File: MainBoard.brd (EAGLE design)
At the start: 50 x 50 mm, 47 parts, among them U1 STM32F10XRXT6, X1 53261-03, X2 53261-03, X3 53261-03, X4 53261-03, Y1 8MHz, Y2 32.768kHz

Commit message: płytka
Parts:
- removed C1, C14, C2, C3, C4: 100n, rcl:C0805
- removed C6: 10u, rcl:SMC_A
- removed ETRX357: ETRX357HR, etrx357_logical:ETRX3
- removed G1: CR2032V, battery:CR2032V
- removed SW1: (no value), SparkFun-Electromechanical:DIPSWITCH-02
- removed X1, X2, X3, X4: 53261-03, con-molex:53261-03
- added C22: (no value), rcl:C0805
- added IC3: (no value), SparkFun-PowerIC:SOT223
- added JP1: (no value), SparkFun-Connectors:1X06_LONGPADS
- added JP2, JP3: M05X2SHD, SparkFun-Connectors:2X5-SHROUDED
- added JP4: (no value), SparkFun-Connectors:1X04_LONGPADS
- added JP5, JP6, JP7, JP8: (no value), SparkFun-Connectors:1X03_LONGPADS
- added LED5, LED7, LED8, LED9: (no value), led:CHIPLED_0805
- added R10, R12, R13, R14: (no value), resistor:M0805
- added U$1, U$2: (no value), synergia_logo:SYNERGIA_16MM
- C21: value 100n -> (none)
- LED1, LED2, LED3: device SparkFun-LED (1):LED-1206 -> led:CHIPLED_0805
- R6, R7, R8: value 220 -> (none); device rcl:M0805 -> resistor:M0805
- moved C16 106.9 mm to (45.5, 37.1), flipped to the bottom, turned to 270 degrees
- moved R5 103.0 mm to (56.0, 21.5), turned to 90 degrees
- moved C17 102.4 mm to (37.8, 32.9), flipped to the bottom, turned to 270 degrees
- moved C18 101.3 mm to (43.4, 52.5), flipped to the bottom, turned to 270 degrees
- moved C5 93.2 mm to (26.7, 12.7)
- moved R2? 90.3 mm to (44.6, 42.2), flipped to the bottom, turned to 180 degrees
- moved C7 89.7 mm to (17.8, 12.7)
- moved C15 88.9 mm to (33.9, 38.9), flipped to the bottom, turned to 180 degrees
- moved R2 88.0 mm to (60.6, 22.0), turned to 270 degrees
- moved C19 85.6 mm to (39.2, 48.9), flipped to the bottom, turned to 180 degrees
- moved C13 83.9 mm to (40.8, 32.5), flipped to the bottom, turned to 90 degrees
- moved R4 82.9 mm to (40.0, 22.2), turned to 90 degrees
- moved LED1 81.8 mm to (55.9, 55.6), turned to 270 degrees
- moved Y2 74.9 mm to (10.2, 25.4), turned to 270 degrees
- moved R1? 74.7 mm to (35.3, 43.1), flipped to the bottom, turned to 90 degrees
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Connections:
- removed net N$11: LED2.C, R8.2
- removed net N$9: LED3.C, R6.2
- removed net RXD: ETRX357.18
- removed net TXD: ETRX357.17
- new net 5V: C21.1, IC3.3, JP5.1, JP6.1, JP7.1, JP8.1
- new net A1: JP2.7, U1.61
- new net A2: JP2.5, U1.62
- new net A3: JP2.9, U1.58
- new net A4: JP2.2, U1.59
- new net A5: JP2.8, U1.39
- new net A6: JP2.10, U1.40
- new net A7: JP2.4, U1.37
- new net A8: JP2.6, U1.38
- new net L1: R7.1, U1.33
- new net L2: R8.1, U1.9
- new net L4: R10.1, U1.15
- new net L6: R12.1, U1.10
- new net L7: R13.1, U1.11
- new net MISO: JP3.9, U1.22
- new net MOSI: JP3.10, U1.23
- new net N$12: LED7.A, R12.2
- new net N$13: LED8.A, R13.2
- new net N$14: LED9.A, R14.2
- new net REG1: JP5.3, U1.41
- new net REG2: JP6.3, U1.42
- new net REG3: JP7.3, U1.43
- new net REG4: JP8.3, U1.44
- new net RX: JP3.5, U1.17
- new net SCK: JP3.8, U1.21
- new net SWO: JP1.6
- new net TX: JP3.6, U1.16
- net 3.3V: now also C22.1, IC3.2, IC3.4, JP1.1, JP2.1, JP3.2, JP4.2, JP4.3, R14.1, R6.1; no longer C1.1, C14.1, C2.1, C21.1, C3.1, C4.1, C6.+, ETRX357.32, SW1.3, SW1.4
- net GND: now also C22.2, IC3.1, JP1.3, JP2.3, JP3.1, JP5.2, JP6.2, JP7.2, JP8.2, LED1.C, LED2.C, LED3.C, LED5.C, LED7.C, LED8.C, LED9.C; no longer C1.2, C14.2, C2.2, C3.2, C4.2, C6.-, ETRX357.1, ETRX357.13, ETRX357.19, ETRX357.20, ETRX357.31, ETRX357.33, G1.-, R6.1, R7.1, R8.1
- net N$1: now also JP4.1; no longer SW1.1
- net N$10: now also LED5.A, R10.2; no longer LED1.C, R7.2
- net N$2: now also JP4.4; no longer SW1.2
- net N$6: now also R6.2; no longer ETRX357.3
- net N$7: now also R7.2; no longer ETRX357.4
- net N$8: now also R8.2; no longer ETRX357.28
- net NRST: now also JP1.5
- net SCL: now also U1.29
- net SDA: now also U1.30
- net SWCLK: now also JP1.2
- net SWDIO: now also JP1.4
- net V_BATT: no longer G1.+
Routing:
- net 3.3V: track 0.00 -> 251.0 mm, vias 0 -> 2
- net NRST: track 0.00 -> 90.1 mm
- net L2: track 0.00 -> 90.1 mm
- net A2: track 0.00 -> 57.5 mm, vias 0 -> 2
- net BOOT0: track 0.00 -> 48.3 mm, vias 0 -> 2
- net BOOT1: track 0.00 -> 48.0 mm, vias 0 -> 2
- net TX: track 0.00 -> 45.8 mm
- net 5V: track 0.00 -> 45.4 mm
- net A1: track 0.00 -> 45.2 mm, vias 0 -> 2
- net REG1: track 0.00 -> 39.5 mm
- net L7: track 0.00 -> 37.9 mm
- net L4: track 0.00 -> 37.4 mm
- net A4: track 0.00 -> 36.8 mm, vias 0 -> 2
- net REG4: track 0.00 -> 36.4 mm
- net REG2: track 0.00 -> 35.9 mm
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- added copper zone on layer 1, net GND
- added copper zone on layer 16, net GND
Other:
- board outline removed

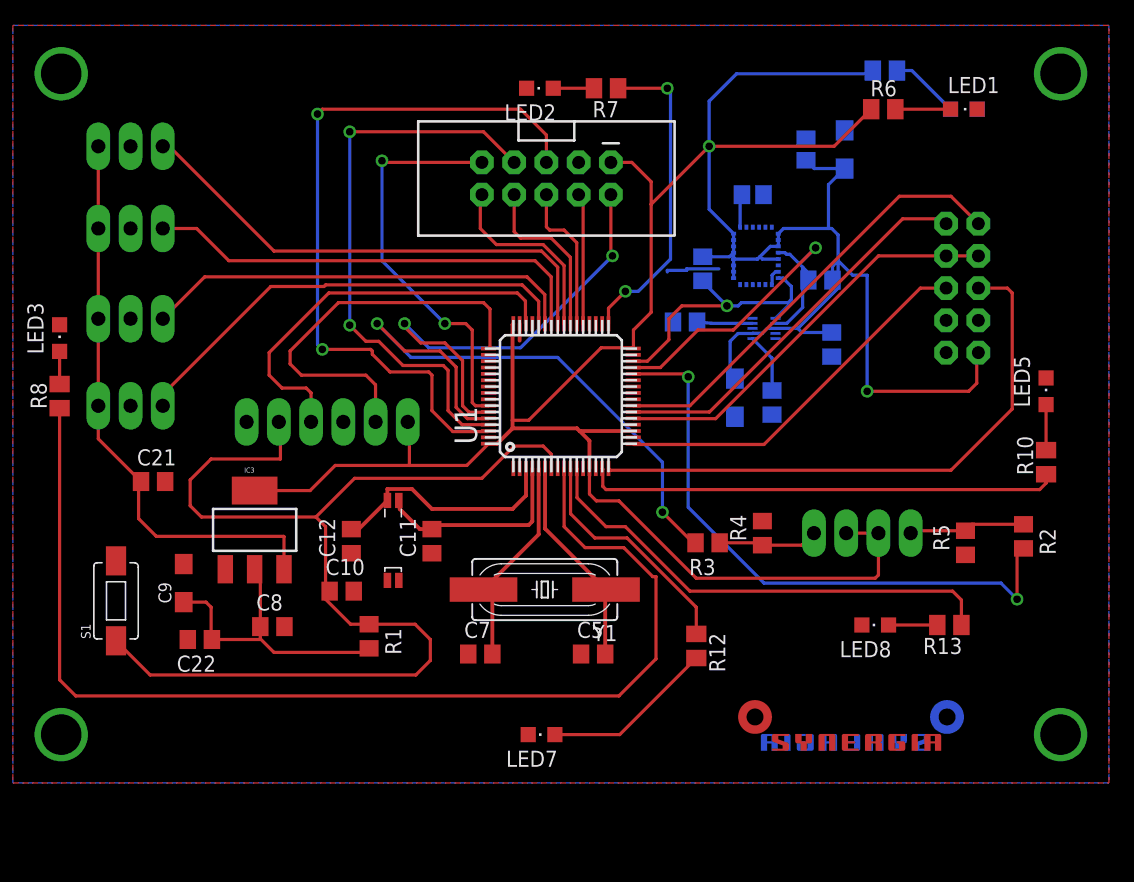
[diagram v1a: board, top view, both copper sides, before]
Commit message: buzzer i adc
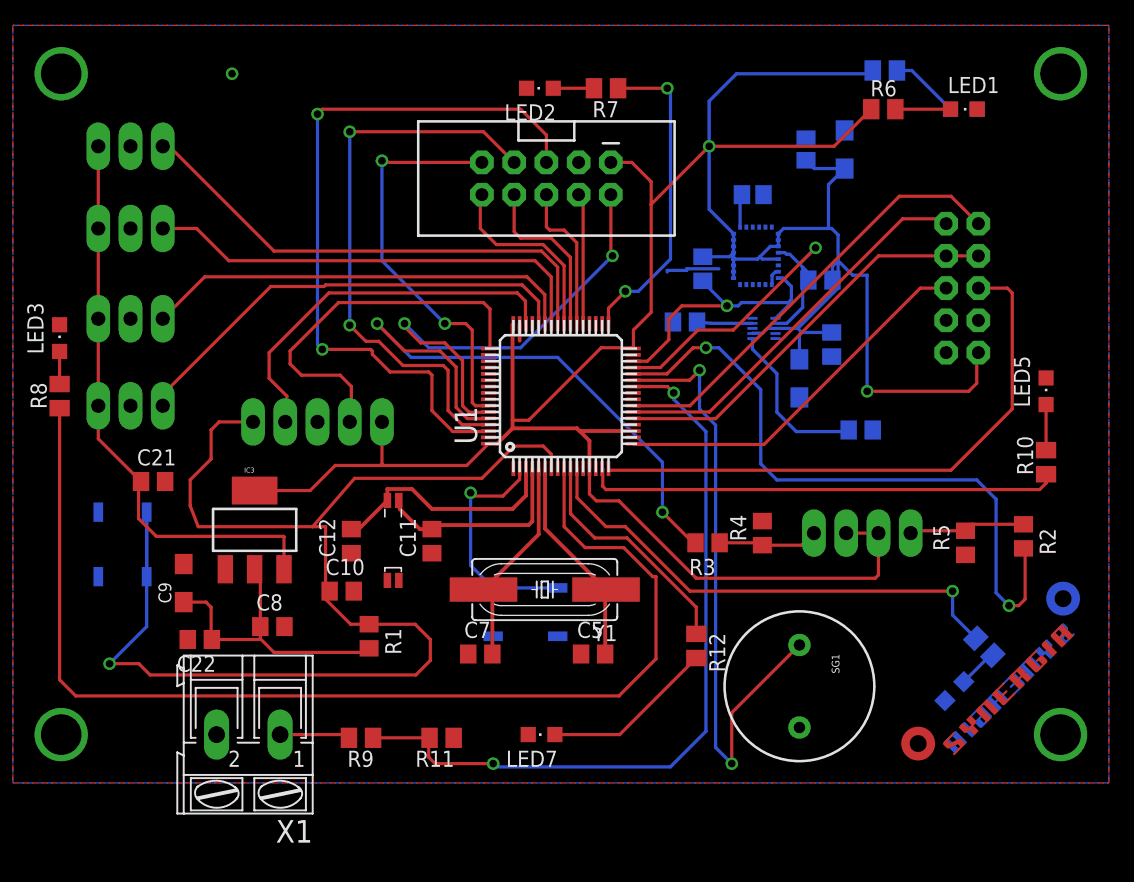
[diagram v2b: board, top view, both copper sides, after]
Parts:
- removed S1: SWITCH-MOMENTARY-2-SMD-1101NE, SparkFun-Electromechanical:TACTILE-SWITCH-1101NE
- added R11, R9: (no value), resistor:M0805
- added S2, S3: (no value), SparkFun-Electromechanical:TACTILE_SWITCH_SMD
- added SG1: BUZZERPTH, SparkFun-Electromechanical:BUZZER-12MM
- added X1: (no value), con-ptr500:AK300/2
- JP1: device SparkFun-Connectors:1X06_LONGPADS -> SparkFun-Connectors:1X05_LONGPADS
- moved U$2 15.3 mm to (66.5, 16.1), turned to 315 degrees
- moved U$1 15.3 mm to (53.2, 2.82), turned to 45 degrees
- moved LED8 8.13 mm to (55.1, 9.77), flipped to the bottom, turned to 225 degrees
- moved C13 7.31 mm to (47.8, 30.4), turned to 0 degrees
- moved C17 5.30 mm to (42.9, 34.4)
- moved R13 3.25 mm to (57.5, 13.3), flipped to the bottom, turned to 225 degrees
- moved JP1 2.03 mm to (10.0, 31.0)
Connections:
- removed net SWO: JP1.6
- new net BUTTON: S3.1, S3.2, U1.2
- new net BUZZ: SG1.-, U1.27
- new net LIPO: R11.2, R9.1, U1.26
- new net N$19: R9.2, X1.1
- net GND: now also R11.1, S2.1, S2.2, S3.3, S3.4, SG1.+, X1.2; no longer S1.P$2
- net NRST: now also S2.3, S2.4; no longer S1.P$1
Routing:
- net LIPO: track 0.00 -> 60.4 mm, vias 0 -> 2
- net BUZZ: track 0.00 -> 49.1 mm, vias 0 -> 2
- net BUTTON: track 0.00 -> 18.7 mm, vias 0 -> 1
- net NRST: track 90.1 -> 106.7 mm, vias 0 -> 1
- net N$4: track 4.73 -> 12.9 mm
- net N$19: track 0.00 -> 5.53 mm
- net BOOT1: track 48.0 -> 52.1 mm
- net 3.3V: track 251.0 -> 248.1 mm
- net SWCLK: track 32.0 -> 30.1 mm
- net SWDIO: track 32.2 -> 30.3 mm
- net L7: track 37.9 -> 39.4 mm, vias 0 -> 1
- net N$13: track 3.84 -> 3.15 mm
- net GND: vias 0 -> 1

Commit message: poprawki
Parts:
- moved LED5 2.90 mm to (63.1, 36.2)
- moved R10 2.41 mm to (63.1, 30.1)
- moved LED2 2.34 mm to (23.0, 59.6)
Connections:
- new net OUT1: JP3.3, U1.35
- new net OUT2: JP3.4, U1.34
- new net SS: JP3.7, U1.20
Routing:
- net OUT1: track 0.00 -> 95.3 mm, vias 0 -> 2
- net OUT2: track 0.00 -> 51.7 mm, vias 0 -> 2
- net SS: track 0.00 -> 30.3 mm
- net L4: track 37.4 -> 40.0 mm
- net L1: track 25.2 -> 23.1 mm
- net SCK: track 32.5 -> 33.6 mm
- net 3.3V: track 248.1 -> 249.0 mm
- net N$10: track 3.59 -> 4.10 mm
